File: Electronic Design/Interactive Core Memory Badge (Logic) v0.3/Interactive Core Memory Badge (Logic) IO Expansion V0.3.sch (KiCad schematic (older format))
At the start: 18 parts, among them J5 Conn_01x04_Female, U5 MCP23017_SO, U6 MCP23017_SO, U8 74HC14, U9 74HC14, X1 SAO_v169bis, X2 SAO_v169bis, X3 SAO_v169bis

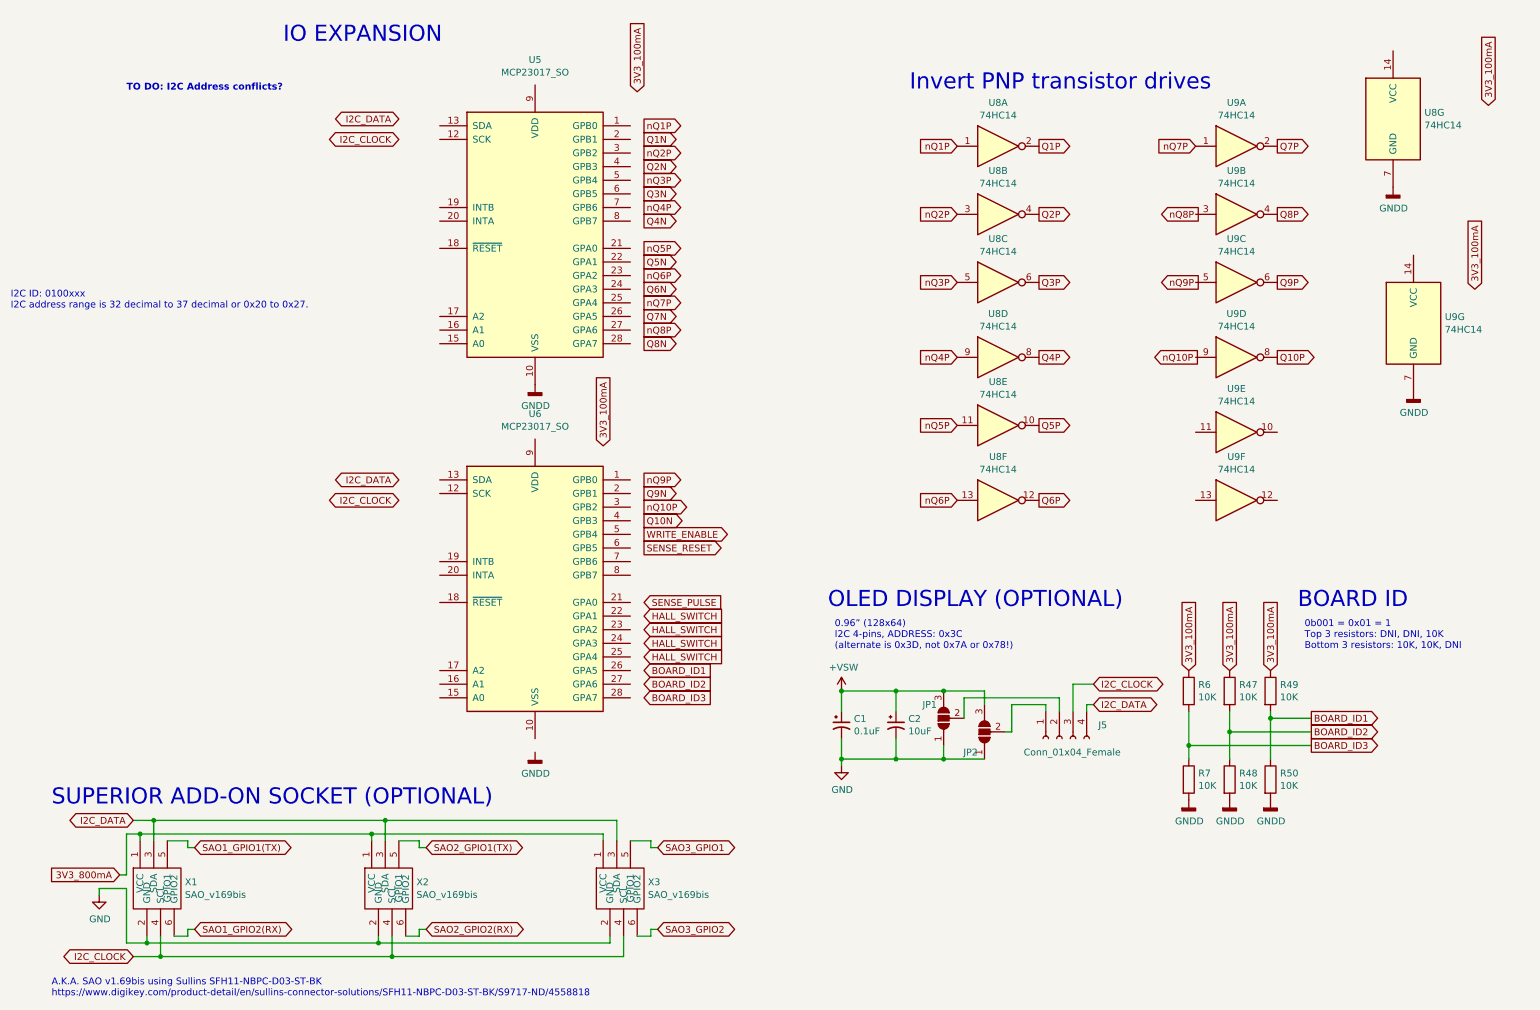
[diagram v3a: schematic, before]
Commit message: Configure IO expanders and I2C addresses
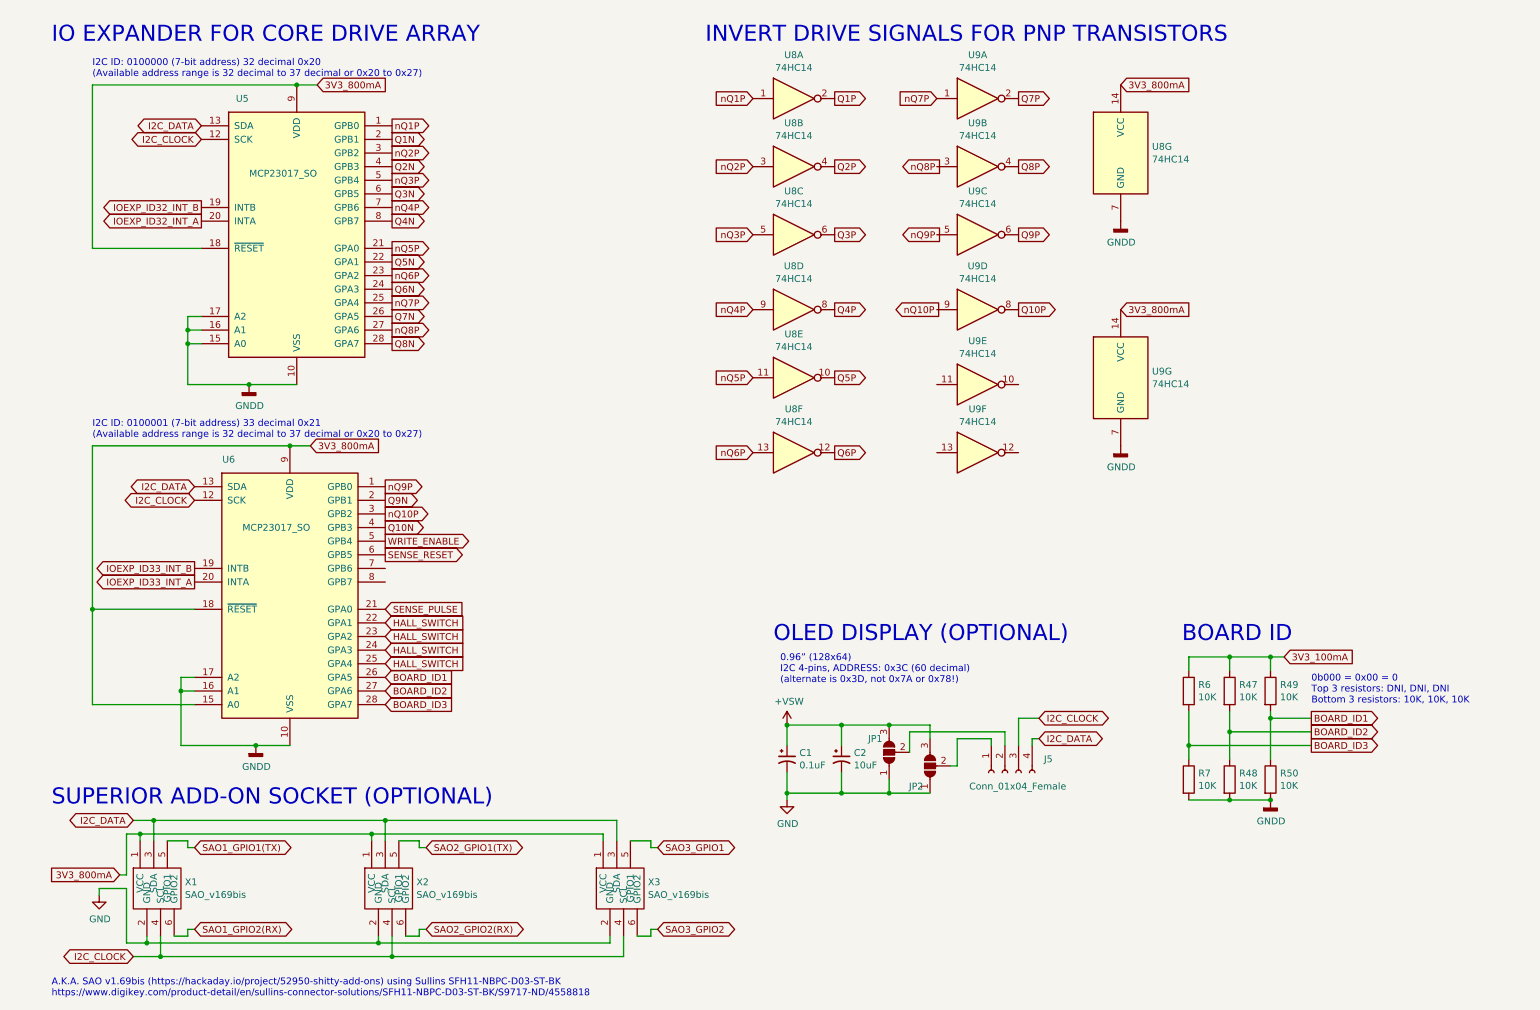
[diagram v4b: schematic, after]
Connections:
- net 3V3_800mA: now also U5.18 (~RESET~), U5.9 (VDD), U6.15 (A0), U6.18 (~RESET~), U6.9 (VDD), U8.14 (VCC), U9.14 (VCC)
- net BOARD_ID1: now also U6.26 (GPA5)
- net BOARD_ID2: now also U6.27 (GPA6)
- net BOARD_ID3: now also U6.28 (GPA7)
- net GNDD: now also U5.15 (A0), U5.16 (A1), U5.17 (A2), U6.10 (VSS), U6.16 (A1), U6.17 (A2)
- net HALL_SWITCH: now also U6.22 (GPA1), U6.23 (GPA2), U6.24 (GPA3), U6.25 (GPA4)
- net I2C_CLOCK: now also U5.12 (SCK), U6.12 (SCK)
- net I2C_DATA: now also U5.13 (SDA), U6.13 (SDA)
- net Q10N: now also U6.4 (GPB3)
- net Q1N: now also U5.2 (GPB1)
- net Q2N: now also U5.4 (GPB3)
- net Q3N: now also U5.6 (GPB5)
- net Q4N: now also U5.8 (GPB7)
- net Q5N: now also U5.22 (GPA1)
- net Q6N: now also U5.24 (GPA3)
- net Q7N: now also U5.26 (GPA5)
- net Q8N: now also U5.28 (GPA7)
- net Q9N: now also U6.2 (GPB1)
- net SENSE_PULSE: now also U6.21 (GPA0)
- net SENSE_RESET: now also U6.6 (GPB5)
- net WRITE_ENABLE: now also U6.5 (GPB4)
- net nQ10P: now also U6.3 (GPB2)
- net nQ1P: now also U5.1 (GPB0)
- net nQ2P: now also U5.3 (GPB2)
- net nQ3P: now also U5.5 (GPB4)
- net nQ4P: now also U5.7 (GPB6)
- net nQ5P: now also U5.21 (GPA0)
- net nQ6P: now also U5.23 (GPA2)
- net nQ7P: now also U5.25 (GPA4)
- net nQ8P: now also U5.27 (GPA6)
- net nQ9P: now also U6.1 (GPB0)
- net IOEXP_ID32_INT_B: now reaches U5.19 (INTB)
- net IOEXP_ID32_INT_A: now reaches U5.20 (INTA)
- net IOEXP_ID33_INT_B: now reaches U6.19 (INTB)
- net IOEXP_ID33_INT_A: now reaches U6.20 (INTA)
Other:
- note added: "0.96” (128x64)\nI2C 4-pins, ADDRESS: 0x3C (60 decimal)\n(alternate is 0x3D, not 0x7A or 0x78!)"
- note added: "0b000 = 0x00 = 0\nTop 3 resistors: DNI, DNI, DNI\nBottom 3 resistors: 10K, 10K, 10K"
- note added: "A.K.A. SAO v1.69bis (https://hackaday.io/project/52950-shitty-add-ons) using Sullins SFH11-NBPC-D03-ST-BK\nhttps://www.digikey.com/product-detail/en/sullins-connector-solutions/SFH11-NBPC-D03-ST-BK/S9717-ND/4558818"
- note added: "I2C ID: 0100000 (7-bit address) 32 decimal 0x20\n(Available address range is 32 decimal to 37 decimal or 0x20 to 0x27)"
- note added: "I2C ID: 0100001 (7-bit address) 33 decimal 0x21\n(Available address range is 32 decimal to 37 decimal or 0x20 to 0x27)"
- note added: "INVERT DRIVE SIGNALS FOR PNP TRANSISTORS"
- note added: "IO EXPANDER FOR CORE DRIVE ARRAY"
- note removed: "0.96” (128x64)\nI2C 4-pins, ADDRESS: 0x3C\n(alternate is 0x3D, not 0x7A or 0x78!)"
- note removed: "0b001 = 0x01 = 1\nTop 3 resistors: DNI, DNI, 10K\nBottom 3 resistors: 10K, 10K, DNI"
- note removed: "A.K.A. SAO v1.69bis using Sullins SFH11-NBPC-D03-ST-BK\nhttps://www.digikey.com/product-detail/en/sullins-connector-solutions/SFH11-NBPC-D03-ST-BK/S9717-ND/4558818"
- note removed: "I2C ID: 0100xxx\nI2C address range is 32 decimal to 37 decimal or 0x20 to 0x27."
- note removed: "IO EXPANSION"
- note removed: "Invert PNP transistor drives"
- note removed: "TO DO: I2C Address conflicts?"
- moved on the sheet: C1, C2, J5, JP1, JP2, U5, U6, U8A, U8B, U8C, U8D, U8E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

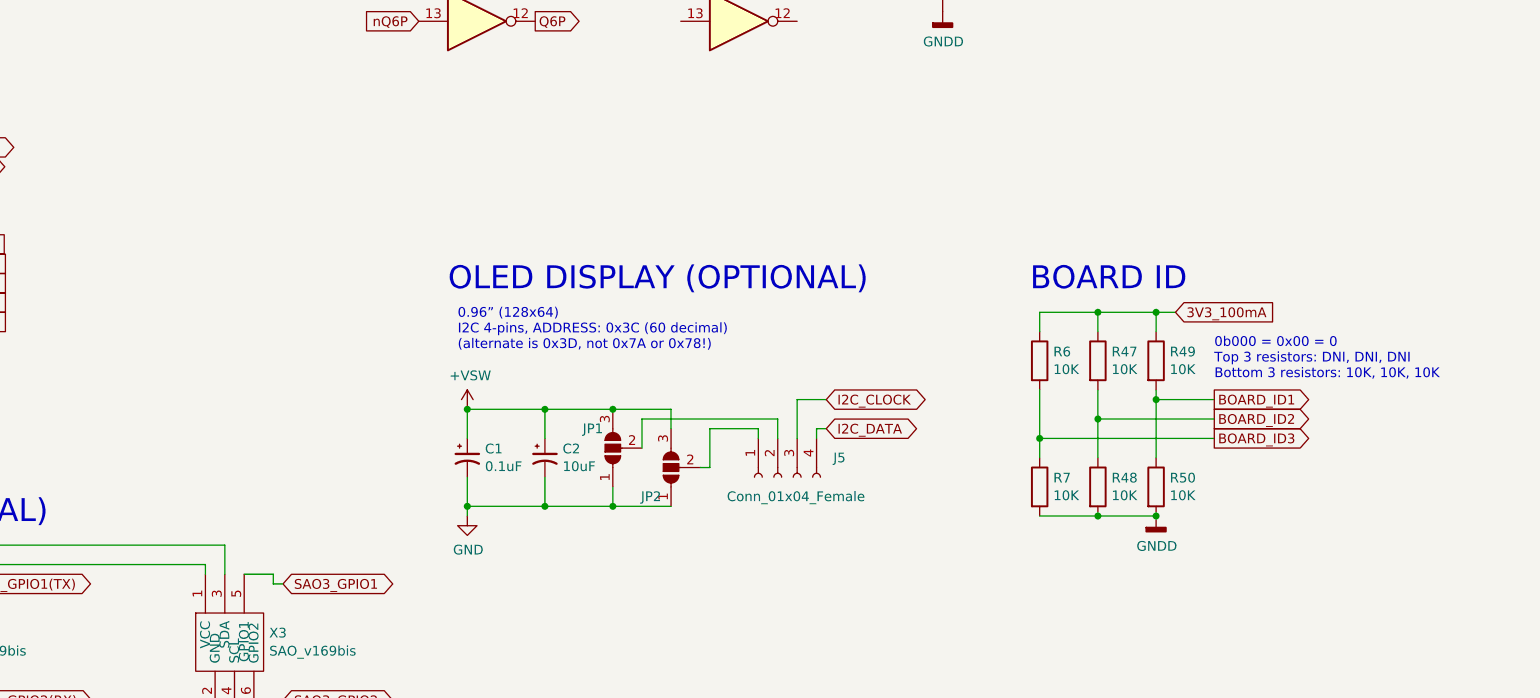
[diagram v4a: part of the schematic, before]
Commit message: Overall PCB layout placements
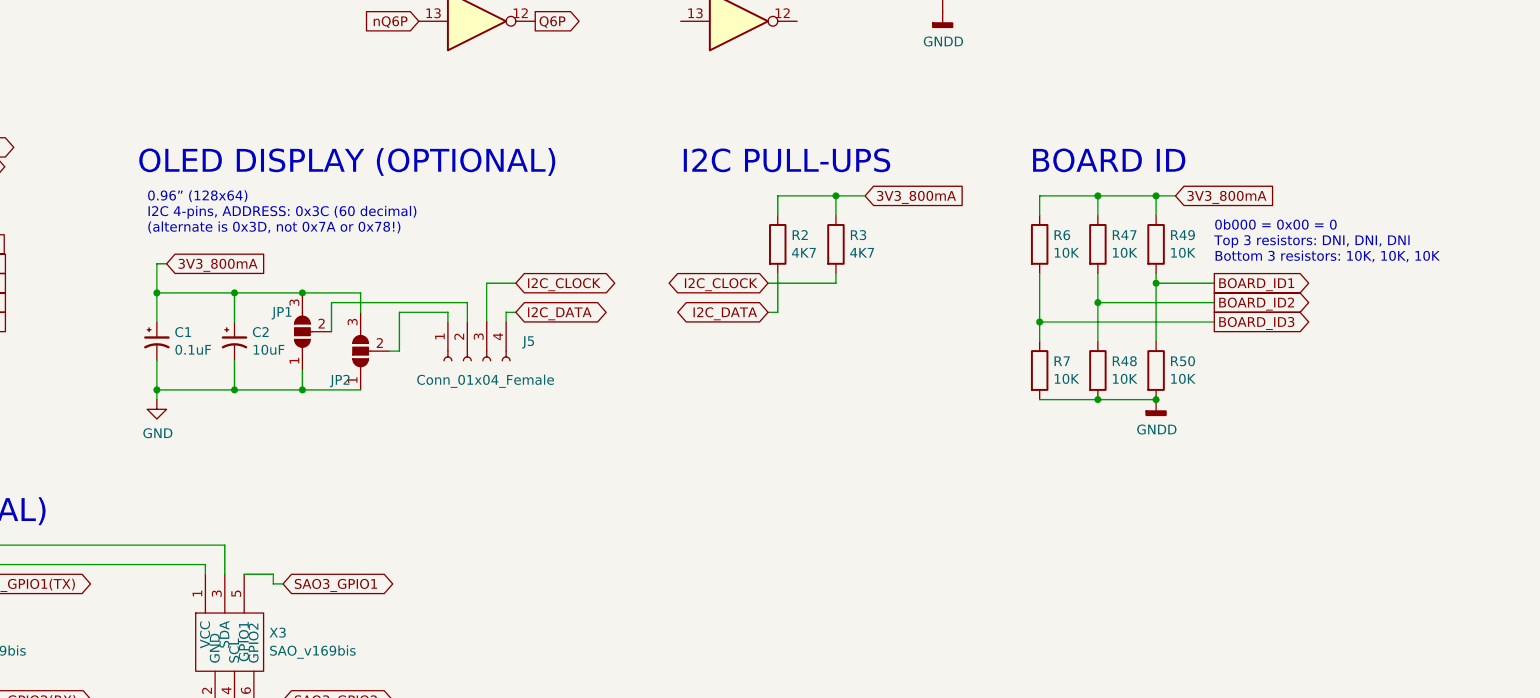
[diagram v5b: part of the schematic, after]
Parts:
- added R2, R3: 4K7, Resistor_SMD:R_0805_2012Metric, symbol Device:R
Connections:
- net +VSW is gone; now on net 3V3_800mA: C1.1, C2.1, JP1.3 (B), JP2.3 (B)
- net 3V3_100mA is gone; now on net 3V3_800mA: R47.1, R49.1, R6.1
- net 3V3_800mA: now also R2.1, R3.1
- net I2C_CLOCK: now also R3.2
- net I2C_DATA: now also R2.2
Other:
- note added: "I2C PULL-UPS"
- moved on the sheet: C1, C2, J5, JP1, JP2, R47, R48, R49, R50, R6, R7

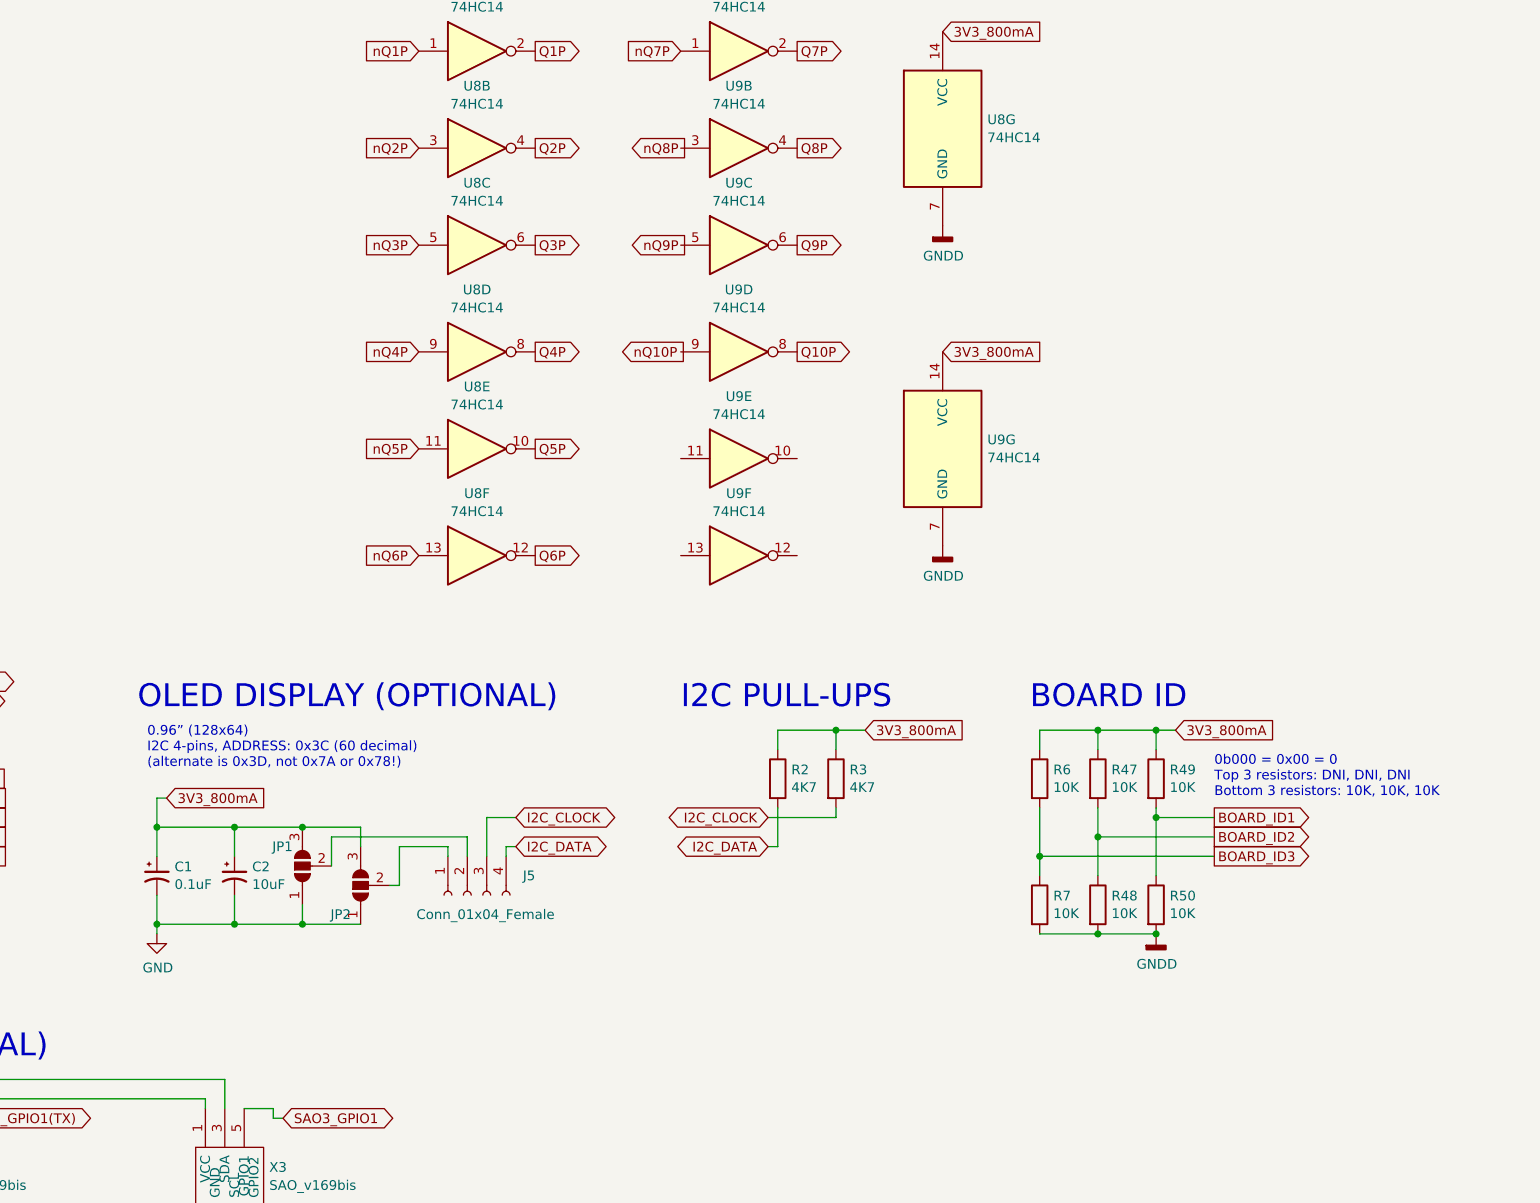
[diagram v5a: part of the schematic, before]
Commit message: Add QWIIC and overall layout updates.
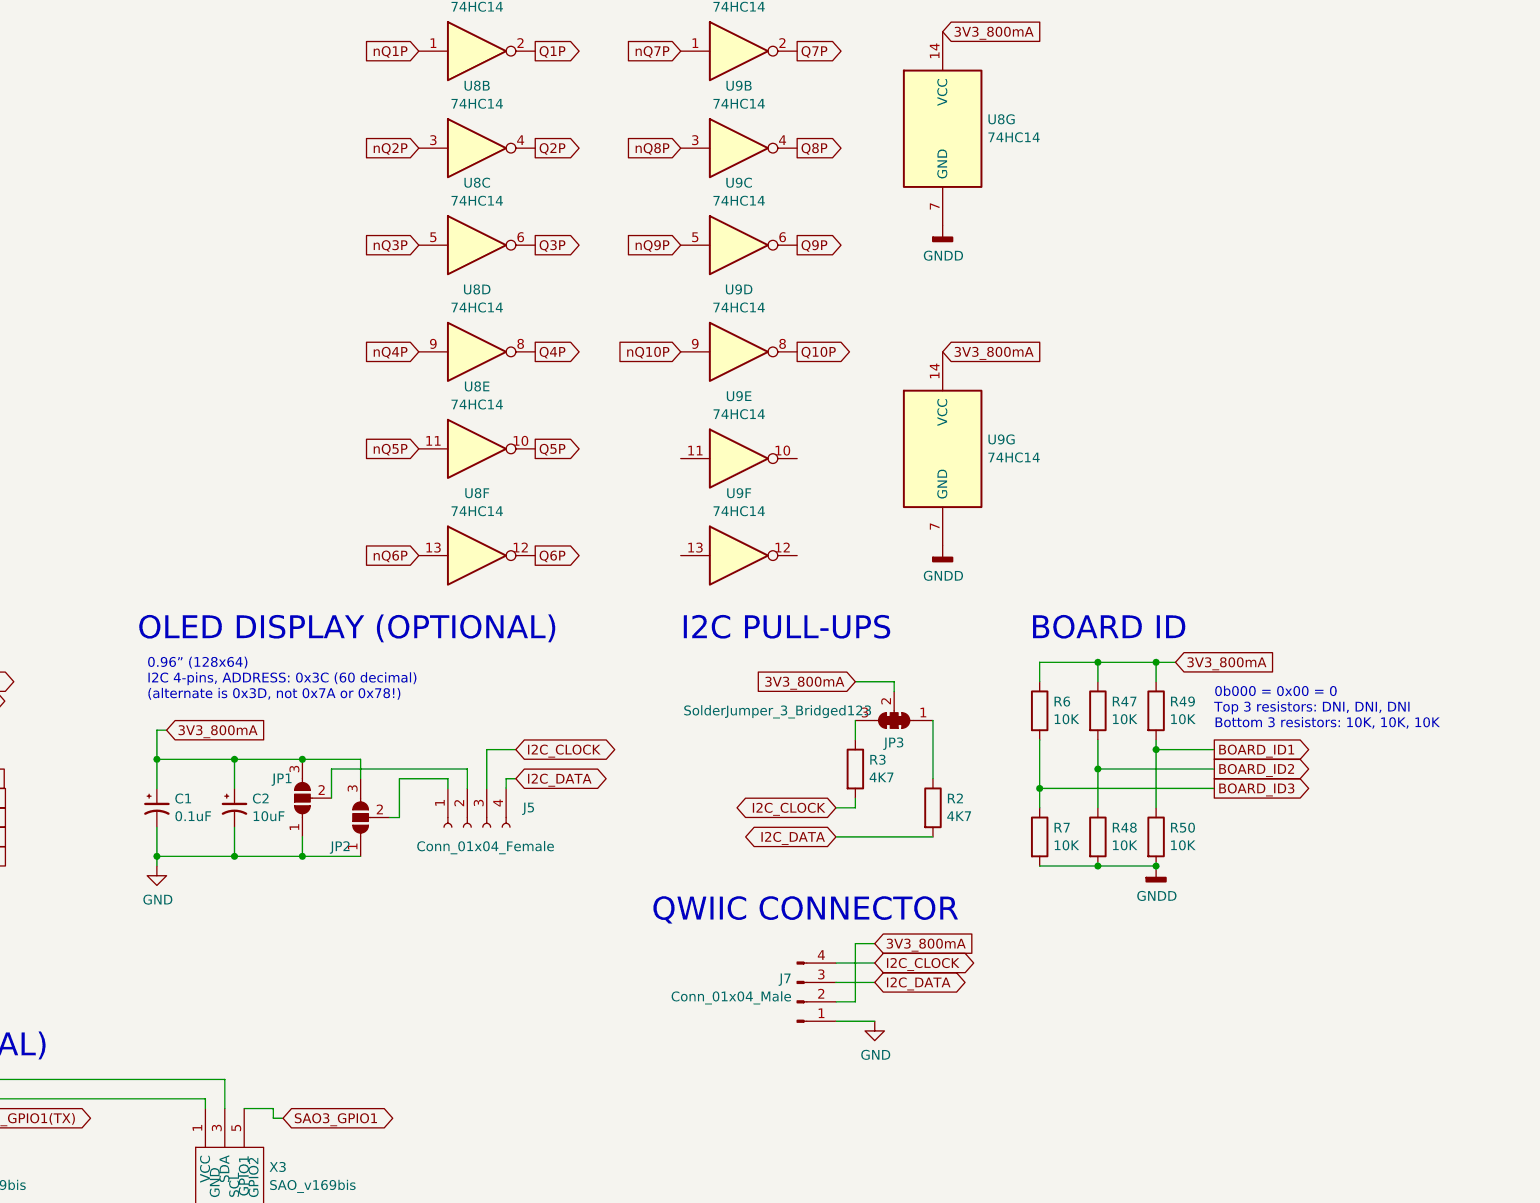
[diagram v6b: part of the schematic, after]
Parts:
- added J7: Conn_01x04_Male, Connector_JST:JST_SH_SM04B-SRSS-TB_1x04-1MP_P1.00mm_Horizontal, symbol Connector:Conn_01x04_Male
- added JP3: SolderJumper_3_Bridged123, Jumper:SolderJumper-3_P1.3mm_Bridged12_Pad1.0x1.5mm_NumberLabels, symbol Jumper:SolderJumper_3_Bridged123
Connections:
- net 3V3_800mA: now also J7.2 (Pin_2), JP3.2 (C); no longer R2.1, R3.1
- net GND: now also J7.1 (Pin_1)
- net I2C_CLOCK: now also J7.4 (Pin_4)
- net I2C_DATA: now also J7.3 (Pin_3)
- net nQ10P: now also U9.9
- net nQ8P: now also U9.3
- net nQ9P: now also U9.5
- new net: JP3.1 (A), R2.1
- new net: JP3.3 (B), R3.1
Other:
- note added: "QWIIC CONNECTOR"
- moved on the sheet: C1, C2, J5, JP1, JP2, R2, R3, R47, R48, R49, R50, R6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
